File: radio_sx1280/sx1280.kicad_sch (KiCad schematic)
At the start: 19 parts, among them J1 Conn_01x08, J2 Conn_01x08, U1 TG-5006Cx, U2 SX1280, U3 2450FM07D0034

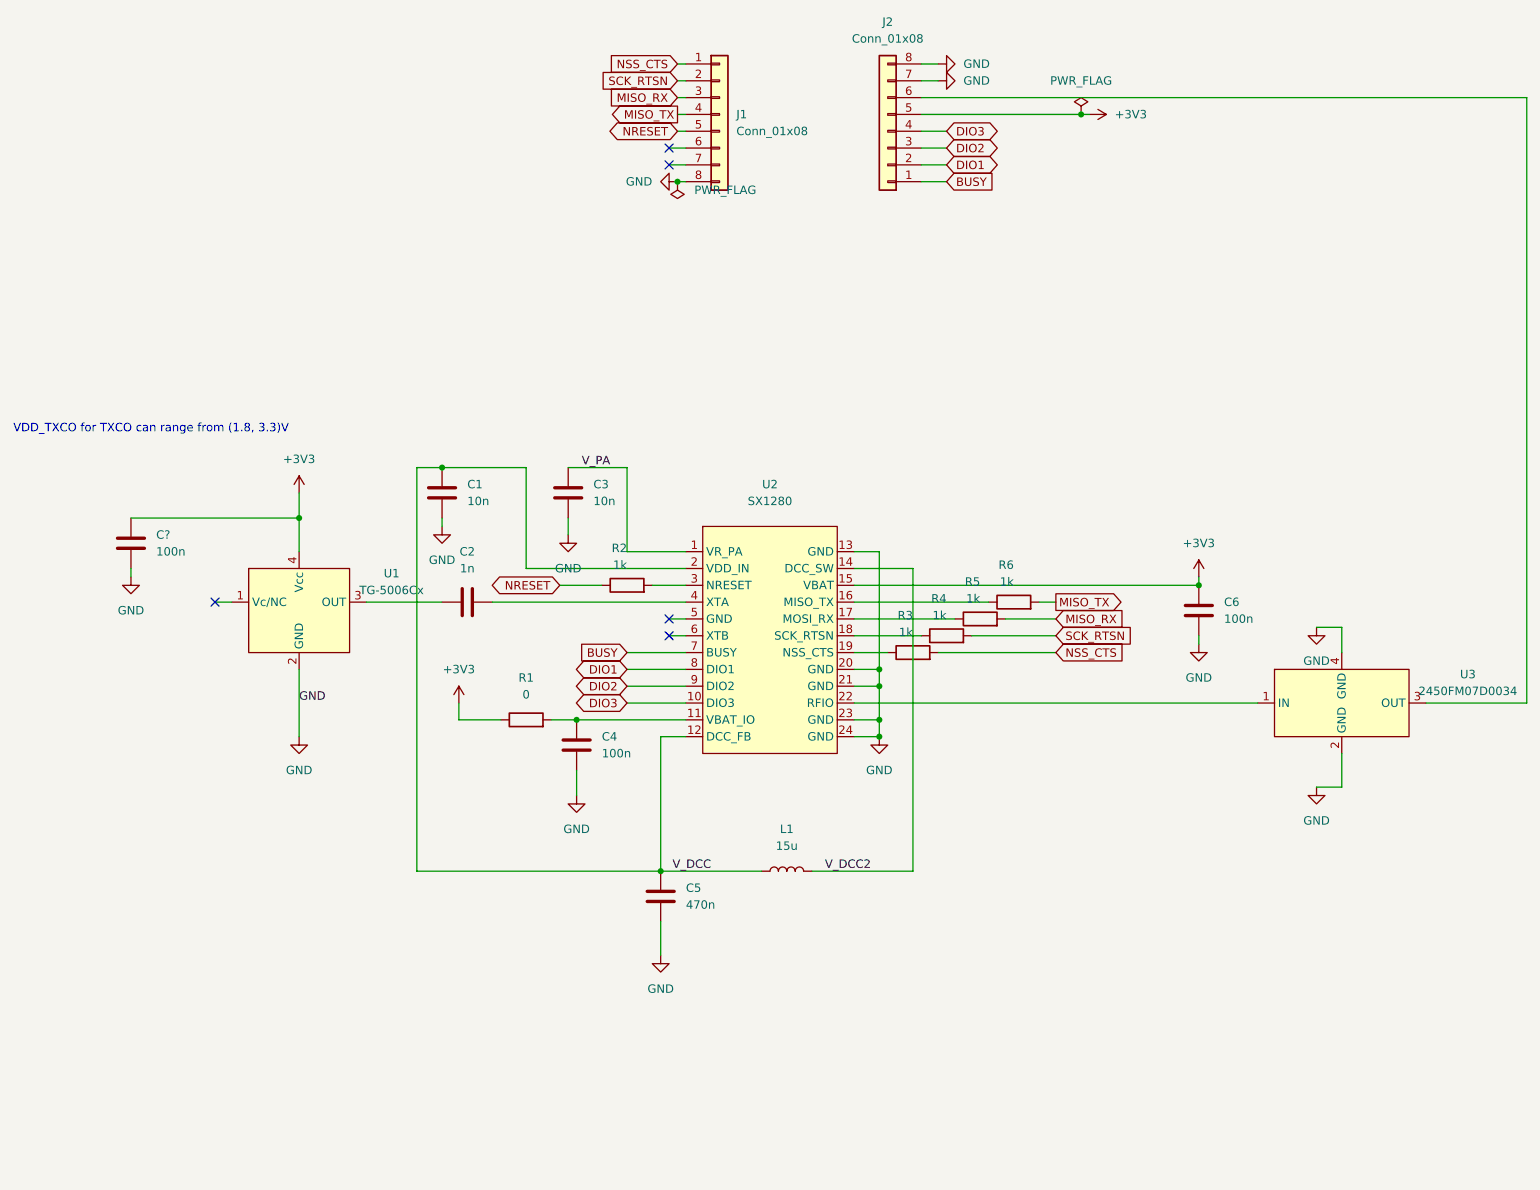
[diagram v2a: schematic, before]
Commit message: tied a nc to ground for txco
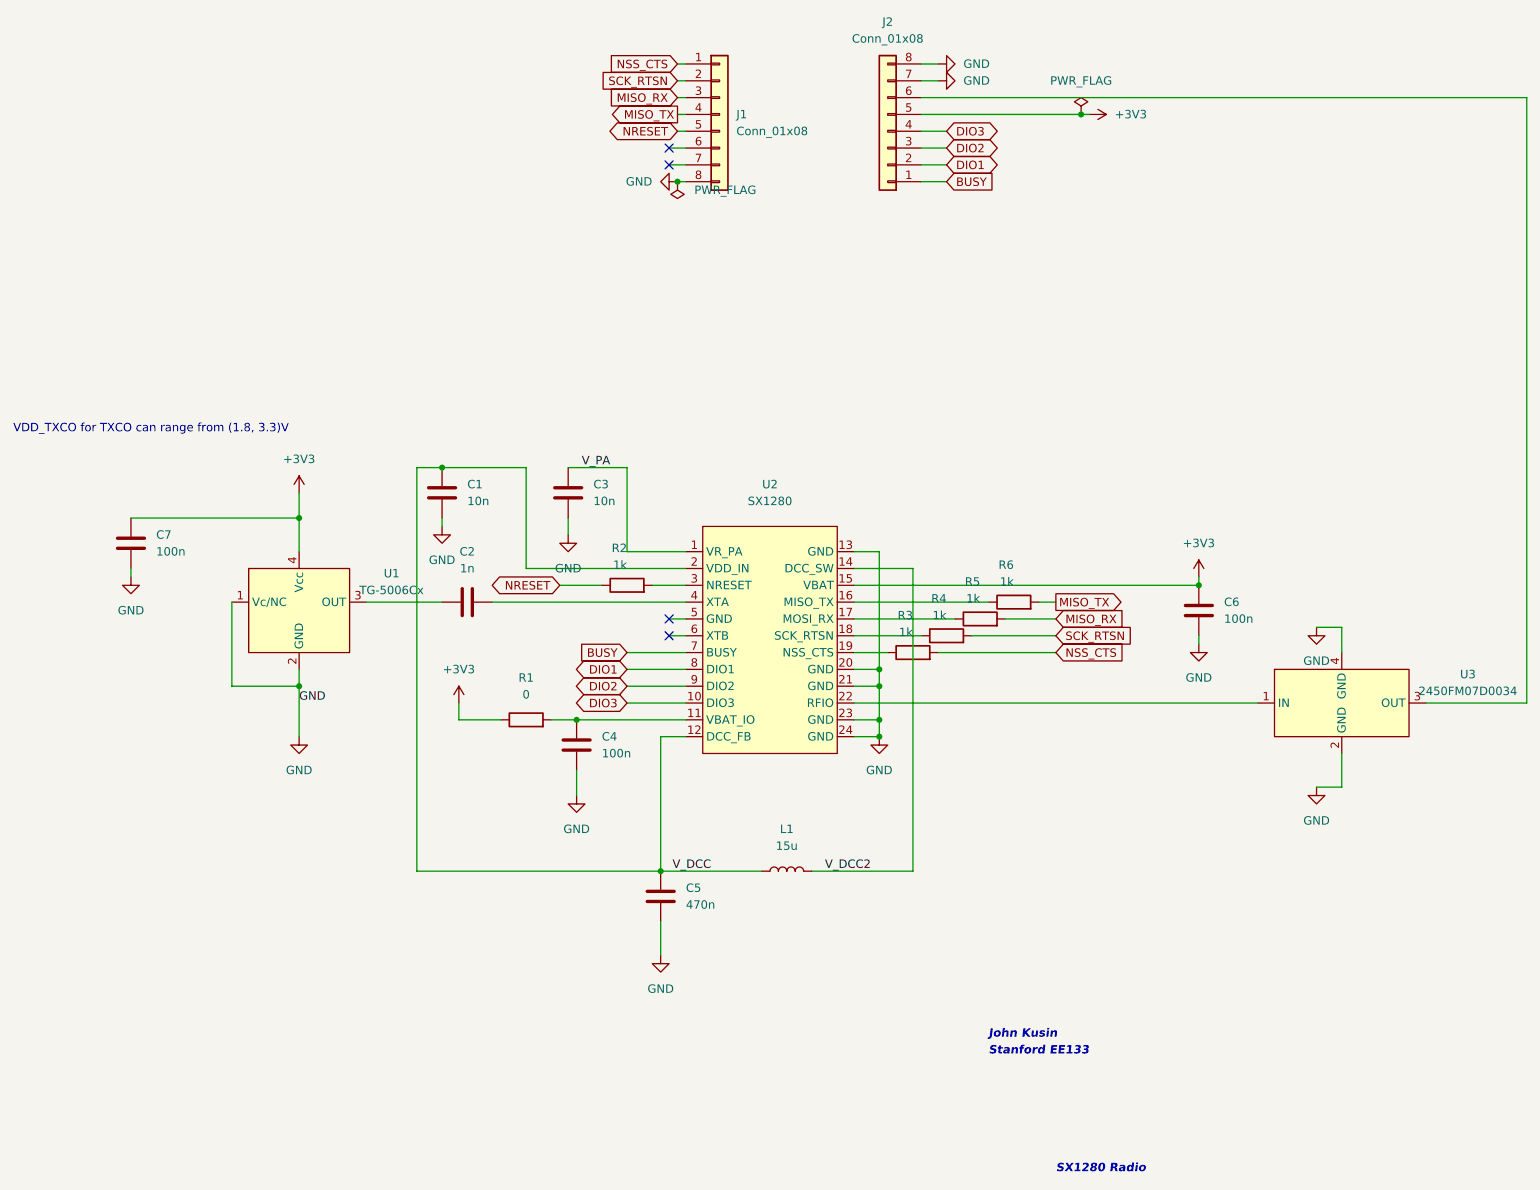
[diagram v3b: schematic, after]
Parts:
- gave numbers to parts that had none: 1
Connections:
- net GND: now also U1.1 (Vc/NC)
- no-connect marks 5 -> 4
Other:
- note added: "John Kusin"
- note added: "SX1280 Radio"
- note added: "Stanford EE133"
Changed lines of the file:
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@@
   (junction (at 130.81 144.78) (diameter 0) (color 0 0 0 0)
+  )
+  (junction (at 76.2 116.84) (diameter 0) (color 0 0 0 0)
   )
   (junction (at 97.79 83.82) (diameter 0) (color 0 0 0 0)
@@
   (no_connect (at 132.08 38.1))
   (no_connect (at 132.08 109.22))
-  (no_connect (at 63.5 104.14))
   (no_connect (at 132.08 35.56))
   (no_connect (at 132.08 106.68))
@@
     (stroke (width 0) (type default) (color 0 0 0 0))
   )
+  (wire (pts (xy 66.04 116.84) (xy 76.2 116.84))
+    (stroke (width 0) (type default) (color 0 0 0 0))
+  )
   (wire (pts (xy 132.08 38.1) (xy 134.62 38.1))
     (stroke (width 0) (type default) (color 0 0 0 0))
@@
     (stroke (width 0) (type default) (color 0 0 0 0))
   )
-  (wire (pts (xy 63.5 104.14) (xy 66.04 104.14))
-    (stroke (width 0) (type default) (color 0 0 0 0))
-  )
   (wire (pts (xy 160.02 104.14) (xy 180.34 104.14))
     (stroke (width 0) (type default) (color 0 0 0 0))
@@
     (stroke (width 0) (type default) (color 0 0 0 0))
   )
-  (wire (pts (xy 76.2 114.3) (xy 76.2 124.46))
+  (wire (pts (xy 76.2 114.3) (xy 76.2 116.84))
     (stroke (width 0) (type default) (color 0 0 0 0))
   )
@@
   )
   (wire (pts (xy 116.84 91.44) (xy 116.84 93.98))
+    (stroke (width 0) (type default) (color 0 0 0 0))
+  )
+  (wire (pts (xy 76.2 116.84) (xy 76.2 124.46))
+    (stroke (width 0) (type default) (color 0 0 0 0))
+  )
+  (wire (pts (xy 66.04 104.14) (xy 66.04 116.84))
     (stroke (width 0) (type default) (color 0 0 0 0))
   )
@@
   (text "VDD_TXCO for TXCO can range from (1.8, 3.3)V" (at 33.02 78.74 0)
     (effects (font (size 1.27 1.27)) (justify left bottom))
+  )
+  (text "SX1280 Radio" (at 190.5 190.5 0)
+    (effects (font (size 1.27 1.27) (thickness 0.254) bold italic) (justify left bottom))
+  )
+  (text "John Kusin" (at 180.34 170.18 0)
+    (effects (font (size 1.27 1.27) bold italic) (justify left bottom))
+  )
+  (text "Stanford EE133" (at 180.34 172.72 0)
+    (effects (font (size 1.27 1.27) bold italic) (justify left bottom))
   )
   (label "GND" (at 76.2 119.38 0)
@@
   (symbol (lib_id "Device:C") (at 50.8 95.25 0) (unit 1)
     (in_bom yes) (on_board yes) (fields_autoplaced)
-    (property "Reference" "C?" (id 0) (at 54.61 93.9799 0)
+    (property "Reference" "C7" (id 0) (at 54.61 93.9799 0)
       (effects (font (size 1.27 1.27)) (justify left))
     )
@@
   (symbol (lib_id "power:GND") (at 50.8 100.33 0) (unit 1)
     (in_bom yes) (on_board yes) (fields_autoplaced)
-    (property "Reference" "#PWR?" (id 0) (at 50.8 106.68 0)
+    (property "Reference" "#PWR017" (id 0) (at 50.8 106.68 0)
       (effects (font (size 1.27 1.27)) hide)
     )
@@
     )
     (path "/111c38f7-ec2b-444f-8ec0-61814dc6a219"
-      (reference "#PWR?") (unit 1) (value "GND") (footprint "")
+      (reference "#PWR017") (unit 1) (value "GND") (footprint "")
     )
     (path "/47782e64-2d17-4f99-a0cc-f4579b8e511b"
@@
     )
     (path "/03542ce4-c372-4a46-bc37-431855927029"
-      (reference "C?") (unit 1) (value "100n") (footprint "")
+      (reference "C7") (unit 1) (value "100n") (footprint "")
     )
     (path "/71ce0edd-2fca-4e62-aacd-1e2fc34784e5"

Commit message: schematic and layout
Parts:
- removed C1, C3: 10n, symbol Device:C
- removed C2: 1n, symbol Device:C
- removed C4, C6, C7: 100n, symbol Device:C
- removed C5: 470n, symbol Device:C
- removed J1, J2: Conn_01x08, symbol Connector_Generic:Conn_01x08
- removed L1: 15u, symbol Device:L
- removed R1: 0, symbol Device:R
- removed R2, R3, R4, R5, R6: 1k, symbol Device:R
- removed U1: TG-5006Cx, symbol Oscillator:TG-5006Cx
- removed U2: SX1280, symbol semtech:SX1280
- removed U3: 2450FM07D0034, symbol RF_Filter:2450FM07D0034
- added C1: 100nF, Capacitor_SMD:C_0402_1005Metric, symbol Device:C_Small
- added C2: 1nF, Capacitor_SMD:C_0402_1005Metric, symbol Device:C_Small
- added C3, C4: 10nF, Capacitor_SMD:C_0402_1005Metric, symbol Device:C_Small
- added C5, C7: 0.1uF, Capacitor_SMD:C_0402_1005Metric, symbol Device:C_Small
- added C6: 470nF, Capacitor_SMD:C_0402_1005Metric, symbol Device:C_Small
- added J1, J10, J11, J12, J13, J14, J15, J16, J2, J3, J4, J5, J6, J7, J8, J9: Conn_01x01, custom-footprints:castellated, symbol Connector_Generic:Conn_01x01
- added L1: 15uH, Inductor_SMD:L_0805_2012Metric, symbol Device:L_Small
- added R1, R2, R3, R4, R5: 1k, Resistor_SMD:R_0402_1005Metric, symbol Device:R_US
- added U1: SX1280IMLTRT, custom-footprints:QFN50P400X400X80-25N-D, symbol symbols:SX1280IMLTRT
- added U2: 2450FM07D0034T, custom-footprints:2450FM07D0034T, symbol RF_Filter:2450FM07D0034
- added U3: TG-5006Cx, Crystal:Crystal_SMD_2520-4Pin_2.5x2.0mm, symbol Oscillator:TG-5006Cx
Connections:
- net +3V3: now also C1.2, C5.1, C7.1, J13.1 (Pin_1), U1.11 (VBAT_IO), U1.15 (VBAT), U3.4 (Vcc)
- net GND: now also C1.1, C3.1, C4.2, C5.2, C6.2, C7.2, J1.1 (Pin_1), J10.1 (Pin_1), J8.1 (Pin_1), U1.13 (GND), U1.20 (GND), U1.21 (GND), U1.23 (GND), U1.24 (GND), U1.25 (GND), U2.2 (GND), U2.4 (GND), U3.1 (Vc/NC), U3.2 (GND)
- net V_DCC: now also C3.2, C6.1, L1.2, U1.12 (DCC_FB), U1.2 (VBAT_IN)
- net V_DCC2: now also L1.1, U1.14 (DCC_SW)
- new net: U1.22 (RFIO), U2.1 (IN)
- new net: J9.1 (Pin_1), U2.3 (OUT)
- new net: C4.1, U1.1 (VR_PA)
- new net: R5.2, U1.16 (MISO_TX)
- new net: R4.2, U1.17 (MOSI_RX)
- new net: R3.2, U1.18 (SCK_RTSN)
- new net: R2.2, U1.19 (NSS_CTS)
- new net: R1.2, U1.3 (NRESET)
- new net: C2.1, U1.4 (XTA)
- new net: C2.2, U3.3 (OUT)
- new net MISO: J2.1 (Pin_1), R5.1
- new net MOSI: J3.1 (Pin_1), R4.1
- new net SCK: J4.1 (Pin_1), R3.1
- new net SX_BUSY: J12.1 (Pin_1), U1.7 (BUSY)
- new net SX_CS: J5.1 (Pin_1), R2.1
- new net SX_DIO1: J15.1 (Pin_1), U1.8 (DIO1)
- new net SX_DIO2: J16.1 (Pin_1), U1.9 (DIO2)
- new net SX_DIO3: J11.1 (Pin_1), U1.10 (DIO3)
- new net SX_RST: J6.1 (Pin_1), R1.1
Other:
- note added: "(Footprint compatible with RFM9x breakouts)"
- note added: "Castellations"
- note added: "Filter"
- note added: "Radio"
- note added: "SX1280 Breakout"
- note added: "TCXO"
- note removed: "John Kusin"
- note removed: "SX1280 Radio"
- note removed: "Stanford EE133"
- note removed: "VDD_TXCO for TXCO can range from (1.8, 3.3)V"
- company: (none) -> Stanford University
- title: (none) -> EE 133 Analog Communications Design Laboratory
